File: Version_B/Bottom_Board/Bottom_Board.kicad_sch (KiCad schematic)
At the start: 17 parts, among them J1 Conn_02x03_Top_Bottom, J2 Conn_01x03_Pin, J3 Screw_Terminal_01x04, J4 DIN-5, J5 Conn_02x03_Top_Bottom, SW1 SW_DIP_x04, U3 ADS1015IDGSR

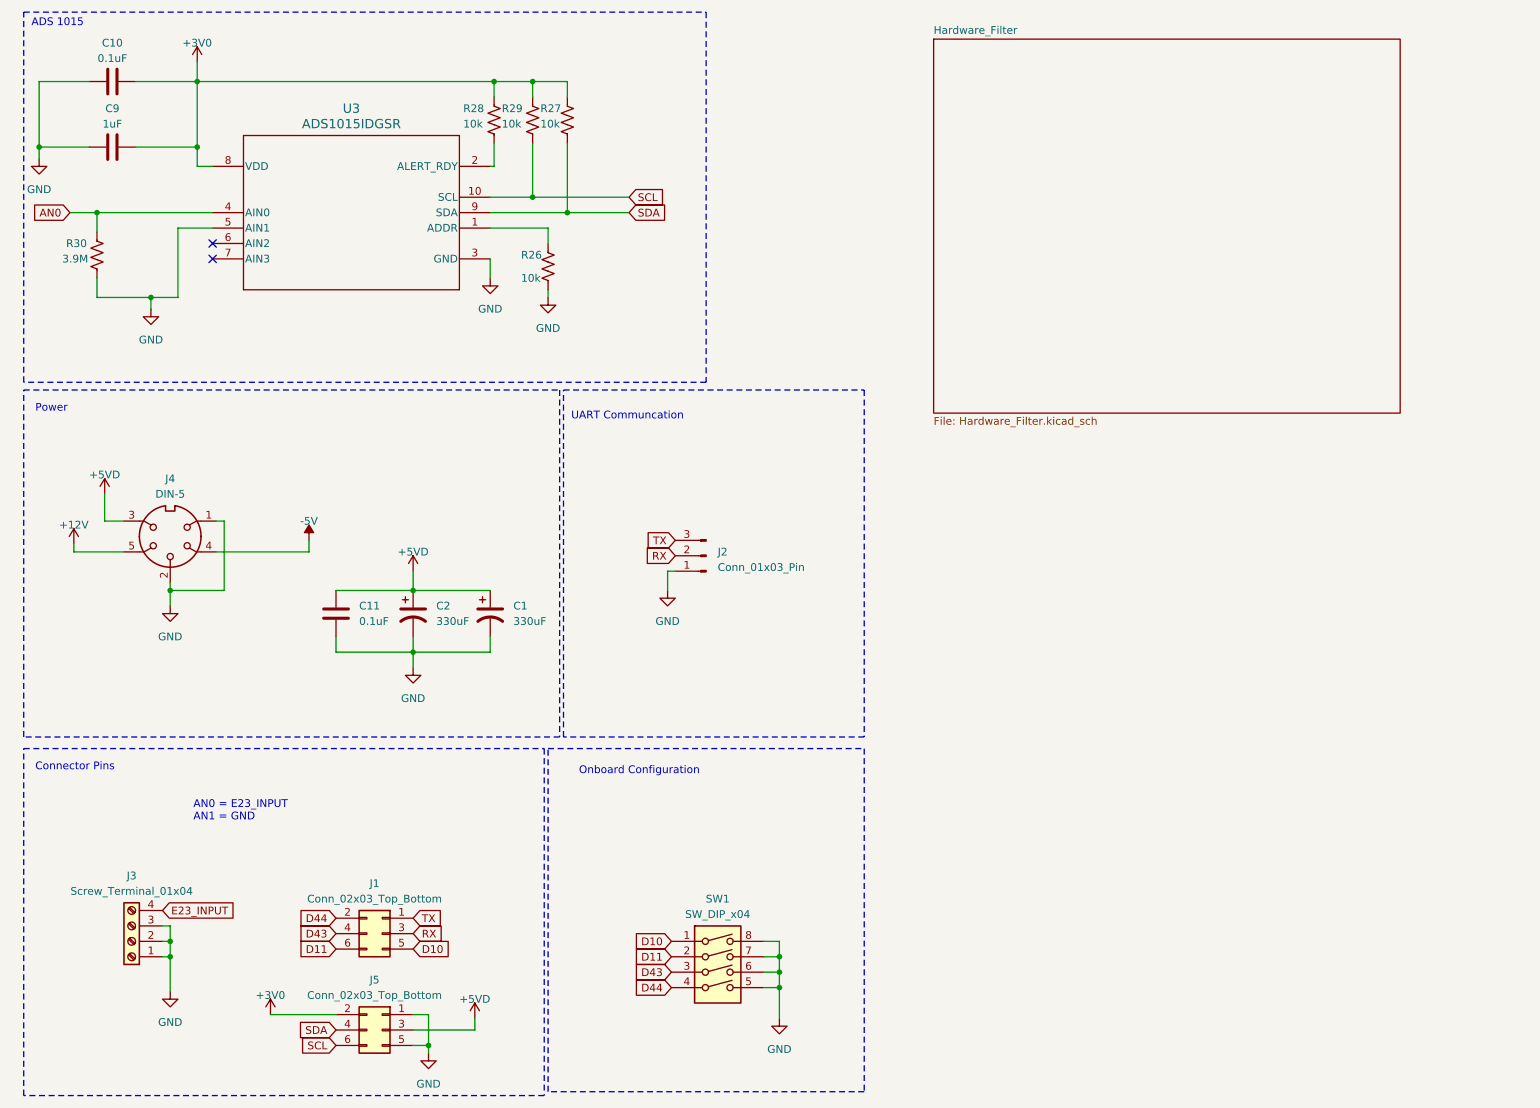
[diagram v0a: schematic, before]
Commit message: added flash folder and adjusted GUI
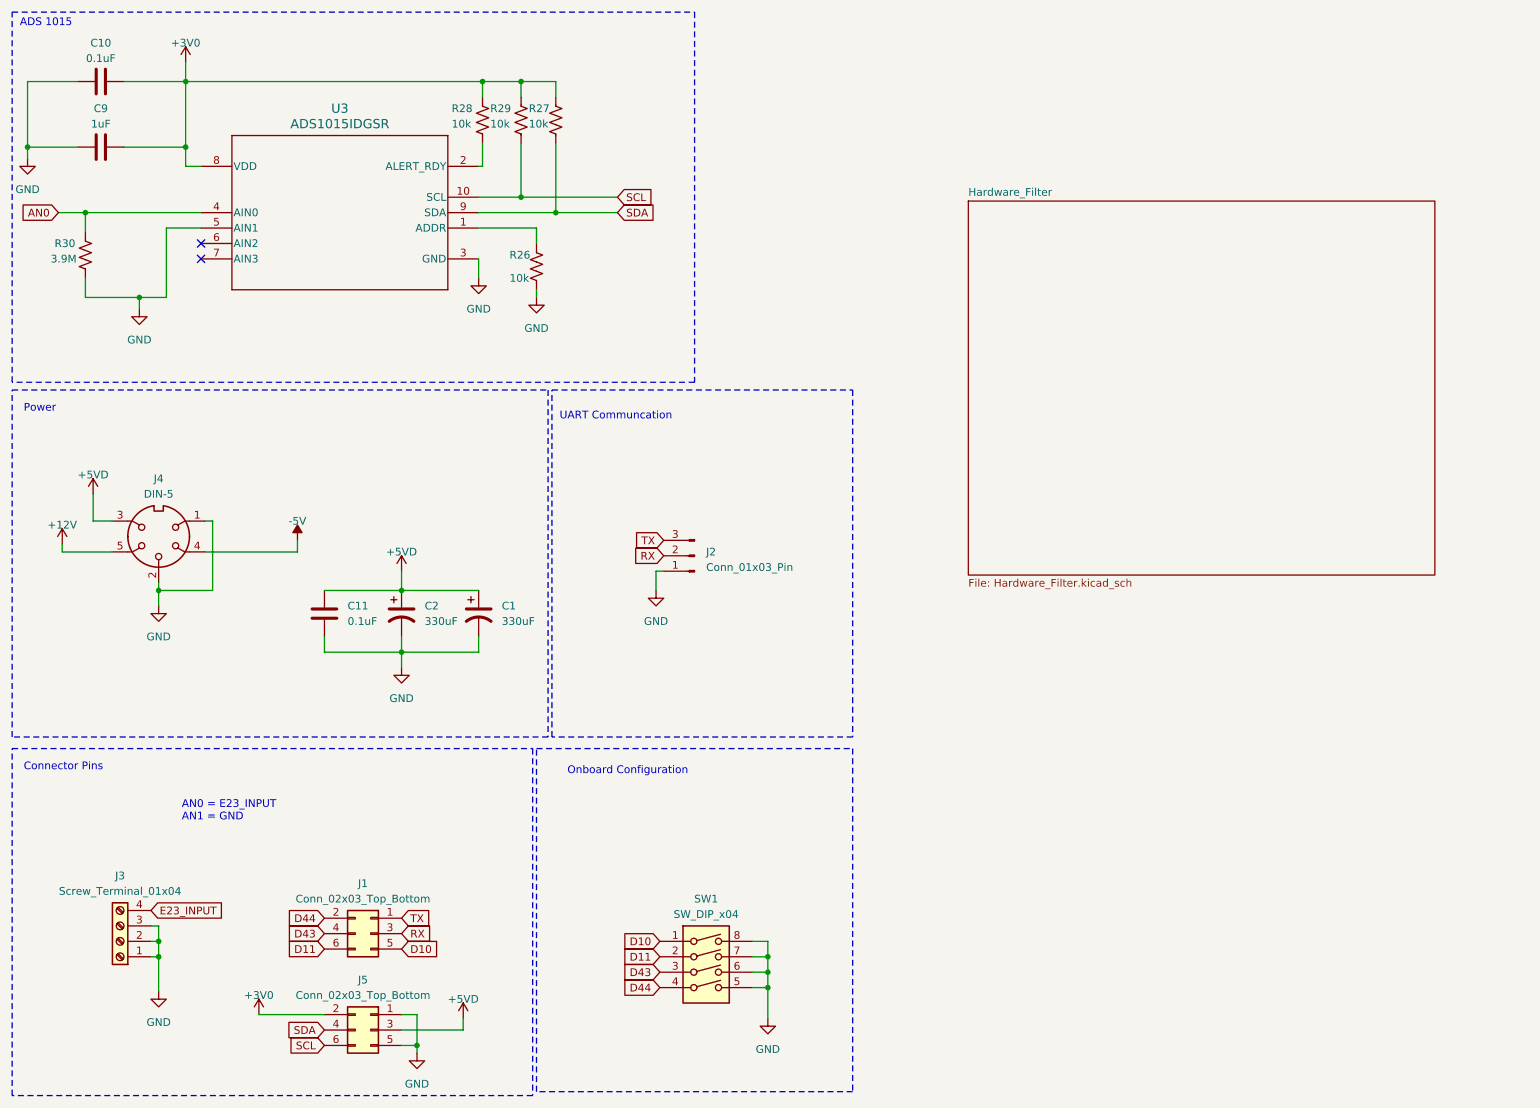
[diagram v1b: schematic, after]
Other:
- title: Monitoring System (Bottom Board) -> Current Monitoring System (Bottom Board)
- moved on the sheet: C1, C10, C11, C2, C9, J1, J2, J3, J4, J5, R26, R27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

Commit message: minor fixe
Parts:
- R26, R27, R28, R29: value 10k -> 10K
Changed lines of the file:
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@@
 			)
 		)
-		(property "Value" "10k"
+		(property "Value" "10K"
 			(at 88.265 33.655 0)
 			(effects
@@
 			)
 		)
-		(property "Value" "10k"
+		(property "Value" "10K"
 			(at 97.79 59.055 0)
 			(effects
@@
 			)
 		)
-		(property "Value" "10k"
+		(property "Value" "10K"
 			(at 100.965 33.655 0)
 			(effects
@@
 			)
 		)
-		(property "Value" "10k"
+		(property "Value" "10K"
 			(at 94.615 33.655 0)
 			(effects

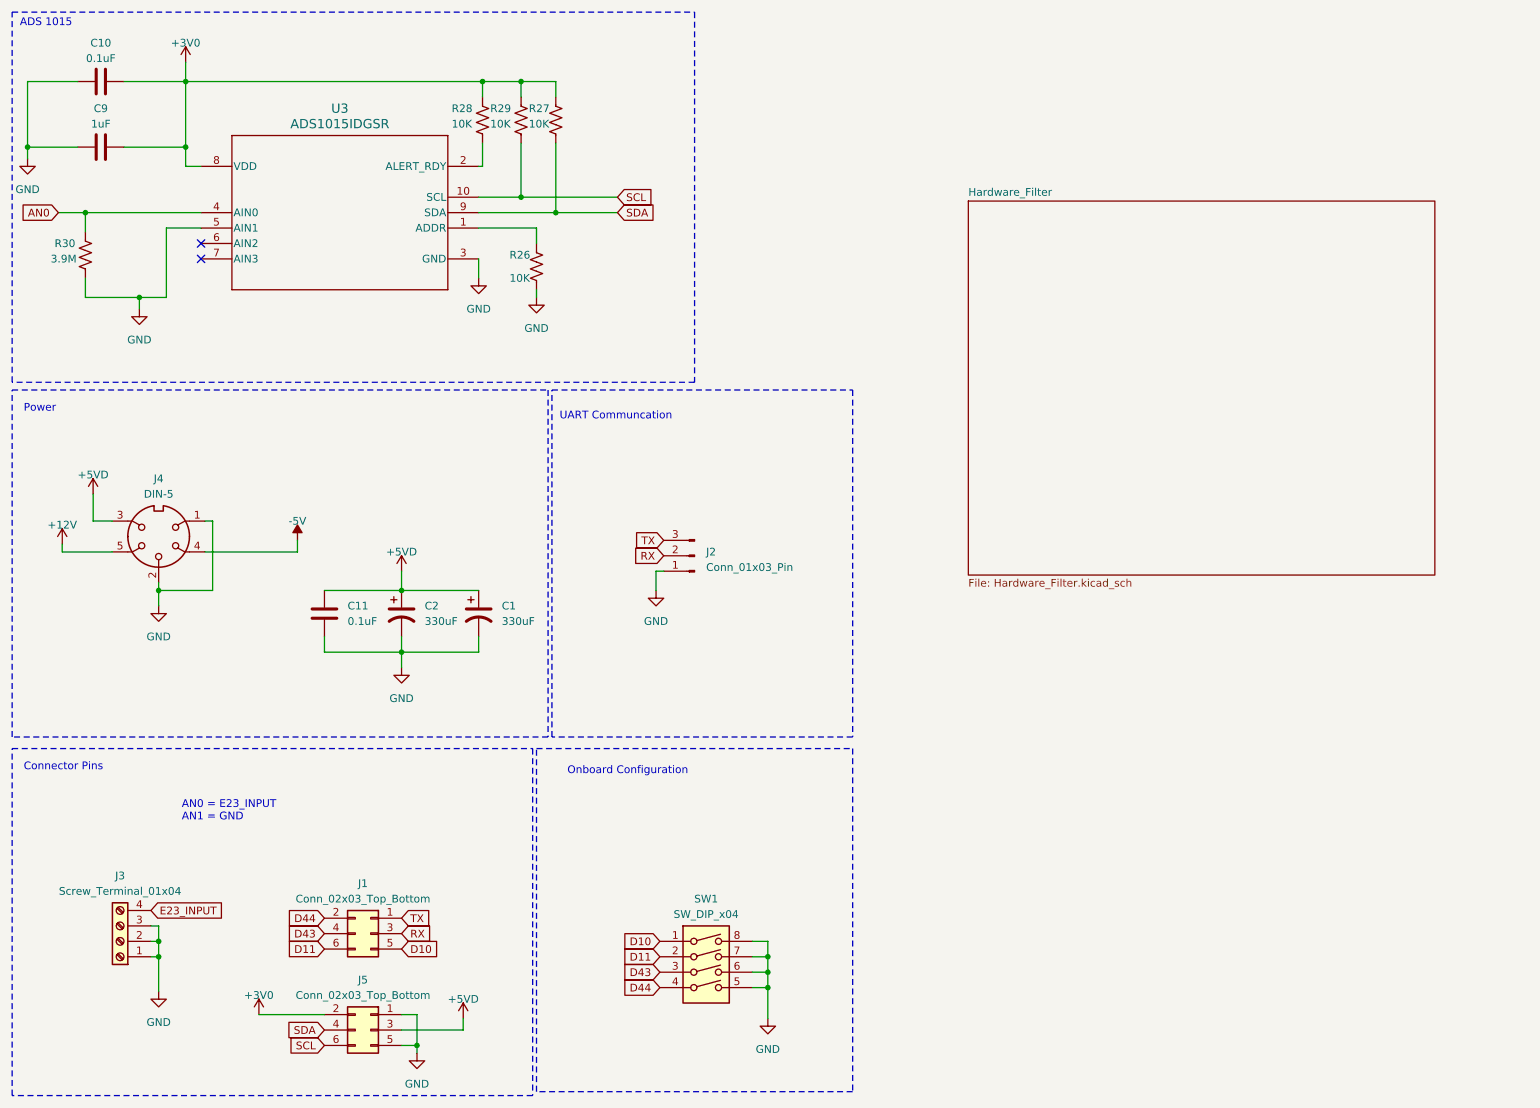
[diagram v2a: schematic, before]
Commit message: fixed directory overwrite
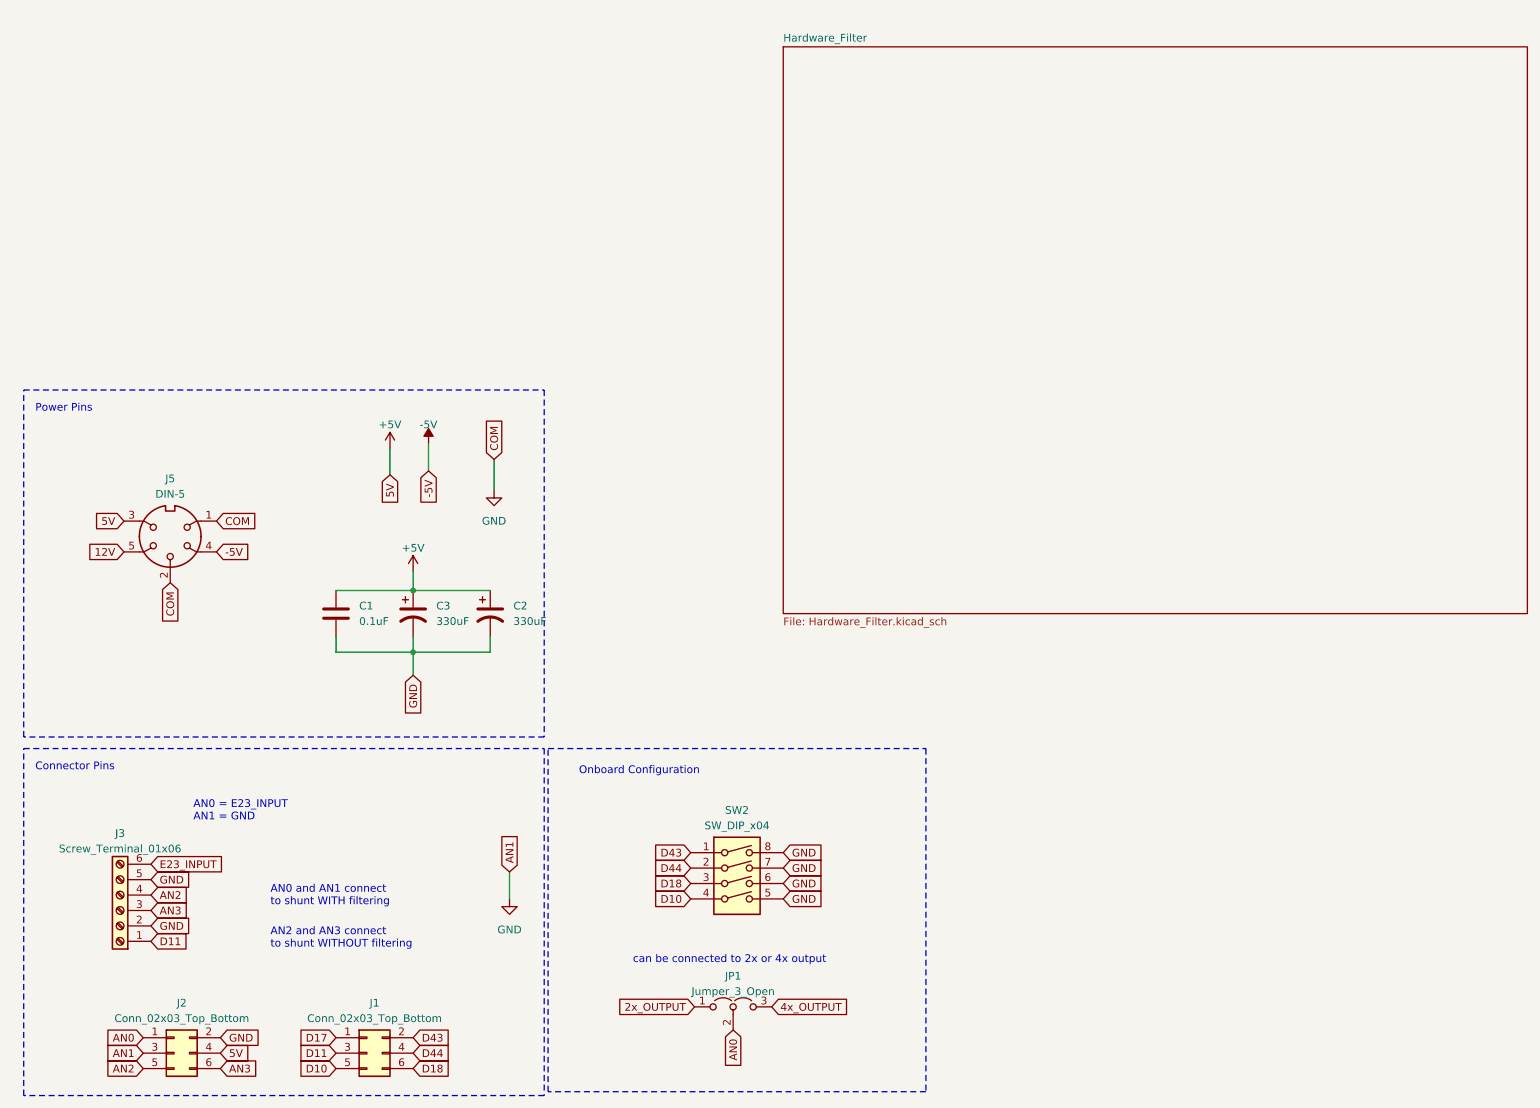
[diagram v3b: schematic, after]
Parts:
- removed C10: 0.1uF, Capacitor_SMD:C_0603_1608Metric, symbol Device:C
- removed C9: 1uF, Capacitor_SMD:C_0603_1608Metric, symbol Device:C
- removed J2: Conn_01x03_Pin, Connector_PinHeader_2.54mm:PinHeader_1x03_P2.54mm_Vertical, symbol Connector:Conn_01x03_Pin
- removed J3: Screw_Terminal_01x04, bot_lib:Terminal_Strip_4_Pin, symbol Connector:Screw_Terminal_01x04
- removed R26, R27, R28, R29: 10K, Resistor_SMD:R_0603_1608Metric, symbol Device:R_US
- removed R30: 3.9M, Resistor_SMD:R_0603_1608Metric, symbol Device:R_US
- removed U3: ADS1015IDGSR, bot_lib:DGS0010A_N, symbol ads1015:ADS1015IDGSR
- added J3: Screw_Terminal_01x06, Connector_Phoenix_MSTB:PhoenixContact_MSTBA_2,5_6-G-5,08_1x06_P5.08mm_Horizontal, symbol Connector:Screw_Terminal_01x06
- added JP1: Jumper_3_Open, Connector_PinHeader_2.54mm:PinHeader_1x03_P2.54mm_Vertical, symbol Jumper:Jumper_3_Open
- J1: renamed from J5; footprint bot_lib:PinSocket_2x03_P2.54mm_Vertical -> Connector_PinSocket_2.54mm:PinSocket_2x03_P2.54mm_Vertical
- J2: renamed from J1; footprint bot_lib:PinSocket_2x03_P2.54mm_Vertical -> Connector_PinSocket_2.54mm:PinSocket_2x03_P2.54mm_Vertical
- renumbered C11 to C1, C1 to C2, C2 to C3, J4 to J5, SW1 to SW2
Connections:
- net +3V0 is gone; now on net D43: J1.2 (Pin_2)
- net RX is gone; now on net GND: J2.3 (Pin_3)
- net SDA is gone; now on net D44: J1.4 (Pin_4)
- net TX is gone; now on net AN0: J2.1 (Pin_1)
- net AN0: now also JP1.2 (C)
- net D10: now also J1.5 (Pin_5), SW2.4; no longer J2.5 (Pin_5), SW2.1
- net D11: now also J1.3 (Pin_3), J3.1 (Pin_1); no longer J2.6 (Pin_6), SW2.2
- net D43: now also SW2.1; no longer J2.4 (Pin_4), SW2.3
- net D44: now also SW2.2; no longer J2.2 (Pin_2), SW2.4
- net E23_INPUT: now also J3.6 (Pin_6)
- net GND: now also J2.2 (Pin_2), J3.2 (Pin_2), J3.5 (Pin_5); no longer J1.1 (Pin_1), J1.5 (Pin_5)
- net +12V renamed 12V
- net +5VD renamed +5V
- net +5V: now also J2.4 (Pin_4); no longer J1.3 (Pin_3)
- net SCL renamed D18
- net D18: now also SW2.3
- new net 2x_OUTPUT: JP1.1 (A)
- new net 4x_OUTPUT: JP1.3 (B)
- new net AN2: J2.5 (Pin_5), J3.4 (Pin_4)
- new net AN3: J2.6 (Pin_6), J3.3 (Pin_3)
- new net D17: J1.1 (Pin_1)
- no-connect marks 2 -> 0
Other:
- note added: "AN0 and AN1 connect to shunt WITH filtering"
- note added: "AN2 and AN3 connect to shunt WITHOUT filtering"
- note added: "Power Pins"
- note added: "can be connected to 2x or 4x output"
- note removed: "ADS 1015"
- note removed: "Power"
- note removed: "UART Communcation"
- company: Secured Solutions Group -> (none)
- title: Current Monitoring System (Bottom Board) -> (none)
- moved on the sheet: C1, C2, C3, J1, J2, J5, SW2

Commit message: updated simulation circuit and finalized hardware design?
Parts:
- removed J3: Screw_Terminal_01x06, Connector_Phoenix_MSTB:PhoenixContact_MSTBA_2,5_6-G-5,08_1x06_P5.08mm_Horizontal, symbol Connector:Screw_Terminal_01x06
- added J3, J6, J7: Conn_01x02_Pin, Connector_PinSocket_2.54mm:PinSocket_1x02_P2.54mm_Vertical, symbol Connector:Conn_01x02_Pin
- added J4: Screw_Terminal_01x05, bot_lib:BarrierStrip_1x05_P8.26mm_3.25in_Vertical, symbol Connector:Screw_Terminal_01x05
- added J8: Screw_Terminal_01x04, Connector_PinHeader_2.54mm:PinHeader_1x04_P2.54mm_Vertical, symbol Connector:Screw_Terminal_01x04
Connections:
- net AN0: now also J8.1 (Pin_1)
- net AN2: now also J4.3 (Pin_3), J8.3 (Pin_3)
- net AN3: now also J4.2 (Pin_2), J8.4 (Pin_4)
- net D10: now also J3.2 (Pin_2)
- net D11: now also J6.2 (Pin_2)
- net D17: now also J7.2 (Pin_2)
- net E23_INPUT: now also J4.5 (Pin_5)
- net GND: now also J3.1 (Pin_1), J4.1 (Pin_1), J4.4 (Pin_4), J6.1 (Pin_1), J7.1 (Pin_1), J8.2 (Pin_2)
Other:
- note added: "Hardware Testing"
- note added: "Undecided Pins for possible future pins, buttons, jumpers, etc."
